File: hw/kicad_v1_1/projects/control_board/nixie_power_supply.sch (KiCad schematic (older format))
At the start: 22 parts, among them Q1 IPB50R199CP, Q2 MMBTA42, Q3 MMBTA42, U1 MAX1771

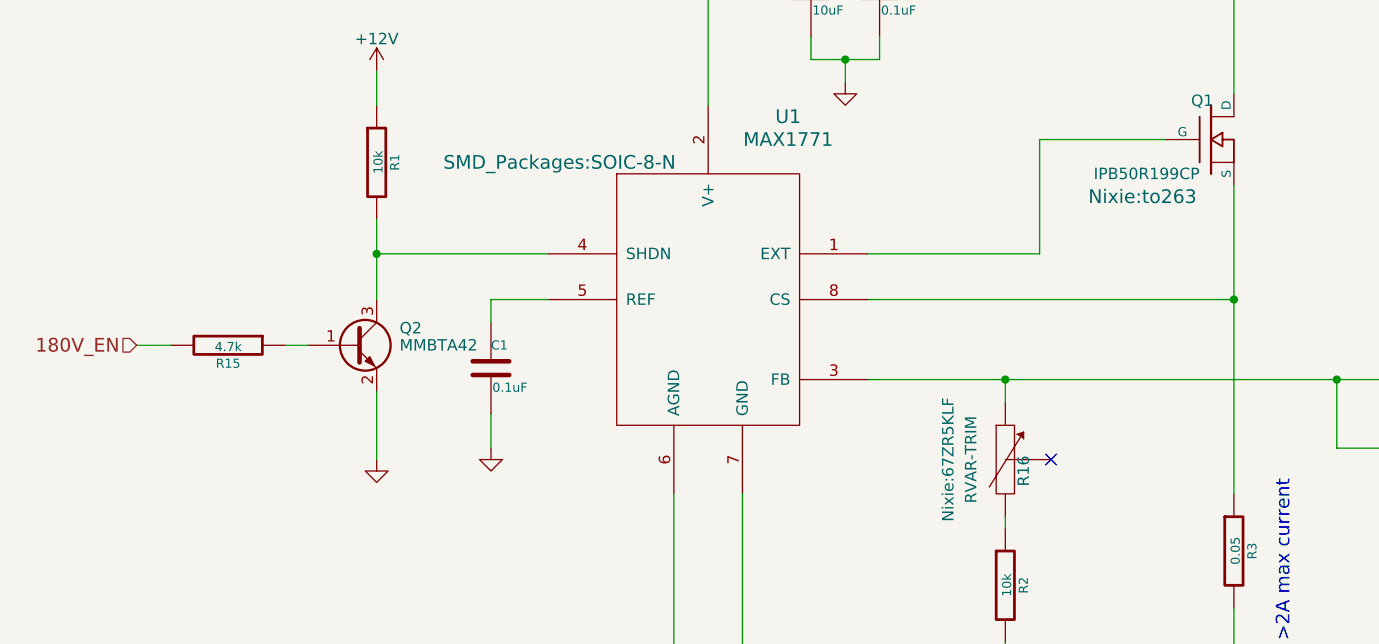
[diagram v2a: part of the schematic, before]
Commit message: Complete with errors
Check in before moving header. Currently the headers don't match up. If
I'm going to connect them with standard header I need to move it
significantly. Check in as a roll back point.
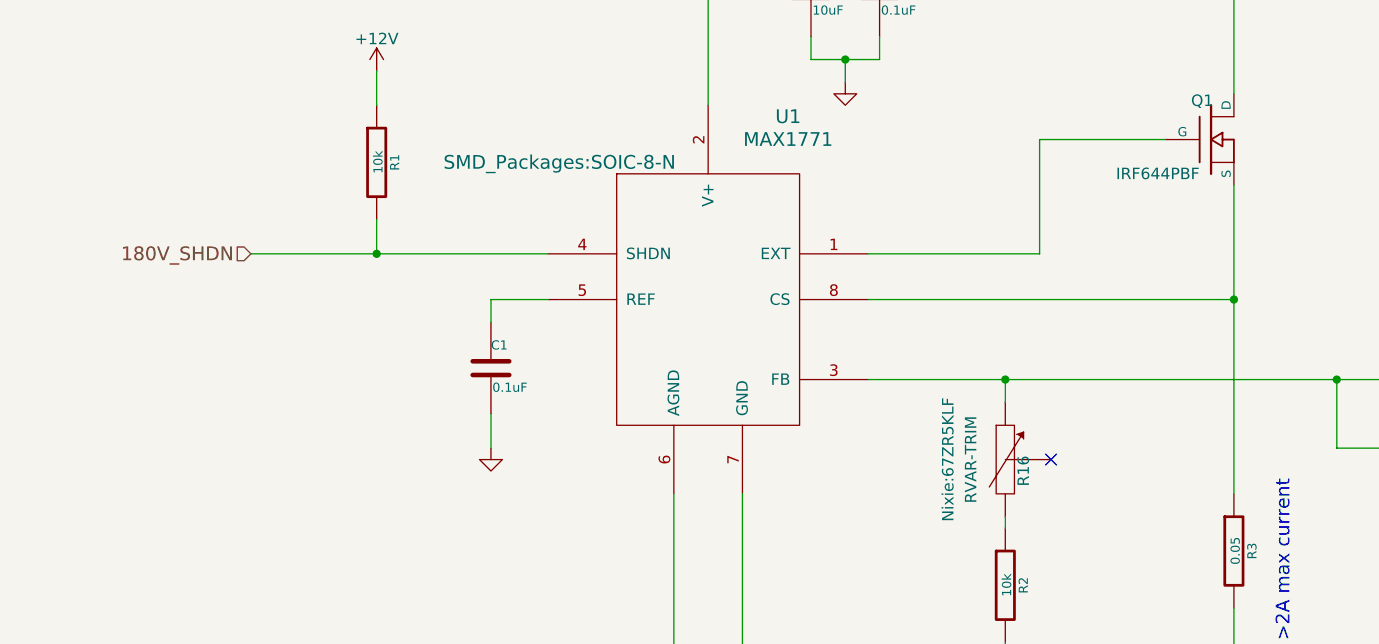
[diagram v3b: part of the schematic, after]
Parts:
- removed Q1: IPB50R199CP, Nixie:to263, symbol IPB50R199CP
- removed Q2: MMBTA42, TO_SOT_Packages_SMD:SOT-23_Handsoldering, symbol MMBTA42
- removed R15: 4.7k, Resistors_SMD:R_0805_HandSoldering, symbol R-RESCUE-nixie_clock
- added Q1: IRF644PBF, TO_SOT_Packages_THT:TO-220_Neutral123_Vertical, symbol MOSFET_N
- R17: footprint Resistors_SMD:R_0805_HandSoldering -> Resistors_SMD:R_1206_HandSoldering
- R3: footprint Resistors_SMD:R_0805_HandSoldering -> Resistors_SMD:R_2512_HandSoldering
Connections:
- net at R3.1, U1.8 (CS): now also Q1.3 (S)
- net 180V_SHDN: now reaches R1.2, U1.4 (SHDN)
- net at D1.2 (A), L1.2: now also Q1.2 (D)
- net at U1.1 (EXT): now also Q1.1 (G)
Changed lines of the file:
@@
 F 0 "R3" V 6080 5600 40  0000 C CNN
 F 1 "0.05" V 6007 5601 40  0000 C CNN
-F 2 "Resistors_SMD:R_0805_HandSoldering" V 5930 5600 30  0001 C CNN
+F 2 "Resistors_SMD:R_2512_HandSoldering" V 5930 5600 30  0001 C CNN
 F 3 "~" H 6000 5600 30  0000 C CNN
 	1    6000 5600
@@
 	1    0    0    -1
 $EndComp
-Text HLabel 1200 4700 0    60   Input ~ 0
-180V_EN
-$Comp
-L IPB50R199CP Q1
-U 1 1 575FC428
-P 5900 3800
-F 0 "Q1" H 5910 3970 50  0000 R CNN
-F 1 "IPB50R199CP" H 5850 3650 50  0000 R CNN
-F 2 "Nixie:to263" H 5600 3550 60  0000 C CNN
-F 3 "" H 5900 3800 60  0000 C CNN
-	1    5900 3800
-	1    0    0    -1
-$EndComp
+Text HLabel 1700 4300 0    60   Input ~ 0
+180V_SHDN
 $Comp
 L +12V #PWR015
@@
 F 0 "R17" V 9930 2750 40  0000 C CNN
 F 1 "470k" V 9857 2751 40  0000 C CNN
-F 2 "Resistors_SMD:R_0805_HandSoldering" V 9780 2750 30  0001 C CNN
+F 2 "Resistors_SMD:R_1206_HandSoldering" V 9780 2750 30  0001 C CNN
 F 3 "~" H 9850 2750 30  0000 C CNN
 	1    9850 2750
@@
 $EndComp
 $Comp
-L GND #PWR019
-U 1 1 57FDE875
-P 2250 5200
-F 0 "#PWR019" H 2250 5200 30  0001 C CNN
-F 1 "GND" H 2250 5130 30  0001 C CNN
-F 2 "" H 2250 5200 60  0000 C CNN
-F 3 "" H 2250 5200 60  0000 C CNN
-	1    2250 5200
-	1    0    0    -1
-$EndComp
-$Comp
-L R-RESCUE-nixie_clock R15
-U 1 1 57FDE8BF
-P 1600 4700
-F 0 "R15" V 1680 4700 40  0000 C CNN
-F 1 "4.7k" V 1607 4701 40  0000 C CNN
-F 2 "Resistors_SMD:R_0805_HandSoldering" V 1530 4700 30  0001 C CNN
-F 3 "~" H 1600 4700 30  0000 C CNN
-	1    1600 4700
-	0    1    1    0
-$EndComp
-$Comp
-L +12V #PWR020
+L +12V #PWR019
 U 1 1 57FDE9DA
 P 2250 3500
-F 0 "#PWR020" H 2250 3350 50  0001 C CNN
+F 0 "#PWR019" H 2250 3350 50  0001 C CNN
 F 1 "+12V" H 2250 3640 50  0000 C CNN
 F 2 "" H 2250 3500 50  0000 C CNN
@@
 $EndComp
 $Comp
-L +180V #PWR021
+L +180V #PWR020
 U 1 1 5820B873
 P 7650 2200
-F 0 "#PWR021" H 7650 2050 60  0001 C CNN
+F 0 "#PWR020" H 7650 2050 60  0001 C CNN
 F 1 "+180V" H 7650 2340 60  0000 C CNN
 F 2 "" H 7650 2200 60  0000 C CNN
@@
 Connection ~ 4300 3450
 Wire Wire Line
-	2250 4150 2250 4500
-Wire Wire Line
 	2250 3500 2250 3650
 Wire Wire Line
@@
 	10100 2750 10250 2750
 Wire Wire Line
-	2250 4900 2250 5200
-Wire Wire Line
-	1850 4700 1950 4700
-Connection ~ 2250 4300
-Wire Wire Line
-	1200 4700 1350 4700
-Wire Wire Line
 	2750 4500 3000 4500
-Wire Wire Line
-	3000 4300 2250 4300
 Wire Wire Line
 	5000 5450 5000 5500
@@
 	6550 2050 6550 2150
 $Comp
-L GND #PWR022
+L GND #PWR021
 U 1 1 58210772
 P 6550 2150
-F 0 "#PWR022" H 6550 2150 30  0001 C CNN
+F 0 "#PWR021" H 6550 2150 30  0001 C CNN
 F 1 "GND" H 6550 2080 30  0001 C CNN
 F 2 "" H 6550 2150 60  0000 C CNN
@@
 $EndComp
 $Comp
-L MMBTA42 Q2
-U 1 1 581FB951
-P 2150 4700
-F 0 "Q2" H 2350 4775 50  0000 L CNN
-F 1 "MMBTA42" H 2350 4700 50  0000 L CNN
-F 2 "TO_SOT_Packages_SMD:SOT-23_Handsoldering" H 2350 4625 50  0001 L CIN
-F 3 "" H 2150 4700 50  0000 L CNN
-	1    2150 4700
-	1    0    0    -1
-$EndComp
-$Comp
 L C-RESCUE-nixie_clock C6
 U 1 1 575BD540
@@
 $EndComp
 NoConn ~ 5200 5200
+$Comp
+L MOSFET_N Q1
+U 1 1 5827D368
+P 5900 3800
+F 0 "Q1" H 5910 3970 50  0000 R CNN
+F 1 "IRF644PBF" H 5850 3650 50  0000 R CNN
+F 2 "TO_SOT_Packages_THT:TO-220_Neutral123_Vertical" V 6050 3900 60  0001 C CNN
+F 3 "" H 5900 3800 60  0000 C CNN
+	1    5900 3800
+	1    0    0    -1
+$EndComp
+Wire Wire Line
+	1700 4300 3000 4300
+Wire Wire Line
+	2250 4150 2250 4300
+Connection ~ 2250 4300
 $EndSCHEMATC

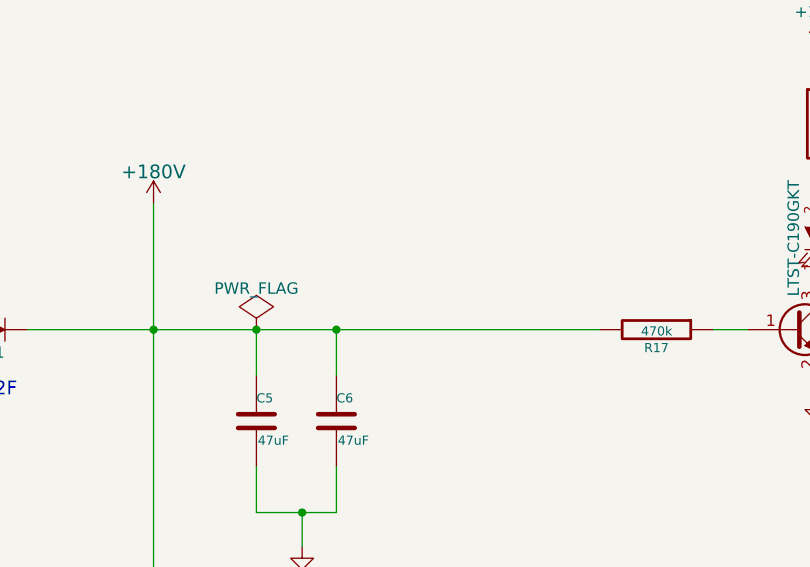
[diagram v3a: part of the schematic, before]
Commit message: Final Release
Update with trimming and bug fixes. This is what is being delivered as a
V1.1.0 release.
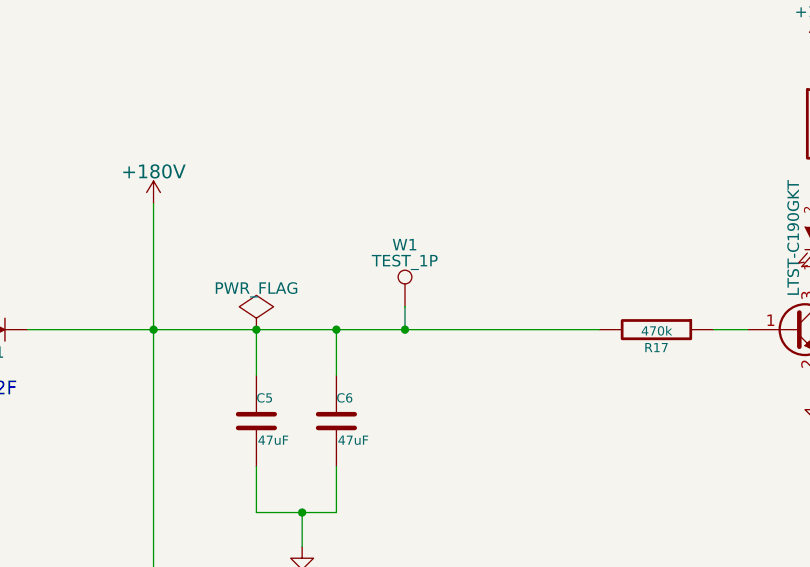
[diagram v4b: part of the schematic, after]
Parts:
- added W1: TEST_1P, Measurement_Points:Measurement_Point_Round-TH_Big, symbol TEST_1P
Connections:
- net +180V: now also W1.1
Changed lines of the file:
@@
 	2250 4150 2250 4300
 Connection ~ 2250 4300
+$Comp
+L TEST_1P W1
+U 1 1 583539E6
+P 8750 2650
+F 0 "W1" H 8750 2920 50  0000 C CNN
+F 1 "TEST_1P" H 8750 2850 50  0000 C CNN
+F 2 "Measurement_Points:Measurement_Point_Round-TH_Big" H 8950 2650 50  0001 C CNN
+F 3 "" H 8950 2650 50  0000 C CNN
+	1    8750 2650
+	1    0    0    -1
+$EndComp
+Wire Wire Line
+	8750 2650 8750 2750
+Connection ~ 8750 2750
 $EndSCHEMATC
